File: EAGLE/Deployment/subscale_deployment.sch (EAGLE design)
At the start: 6 parts, among them J1 1935161, J2 1935161, J3 1935161, Q1 100V 14A

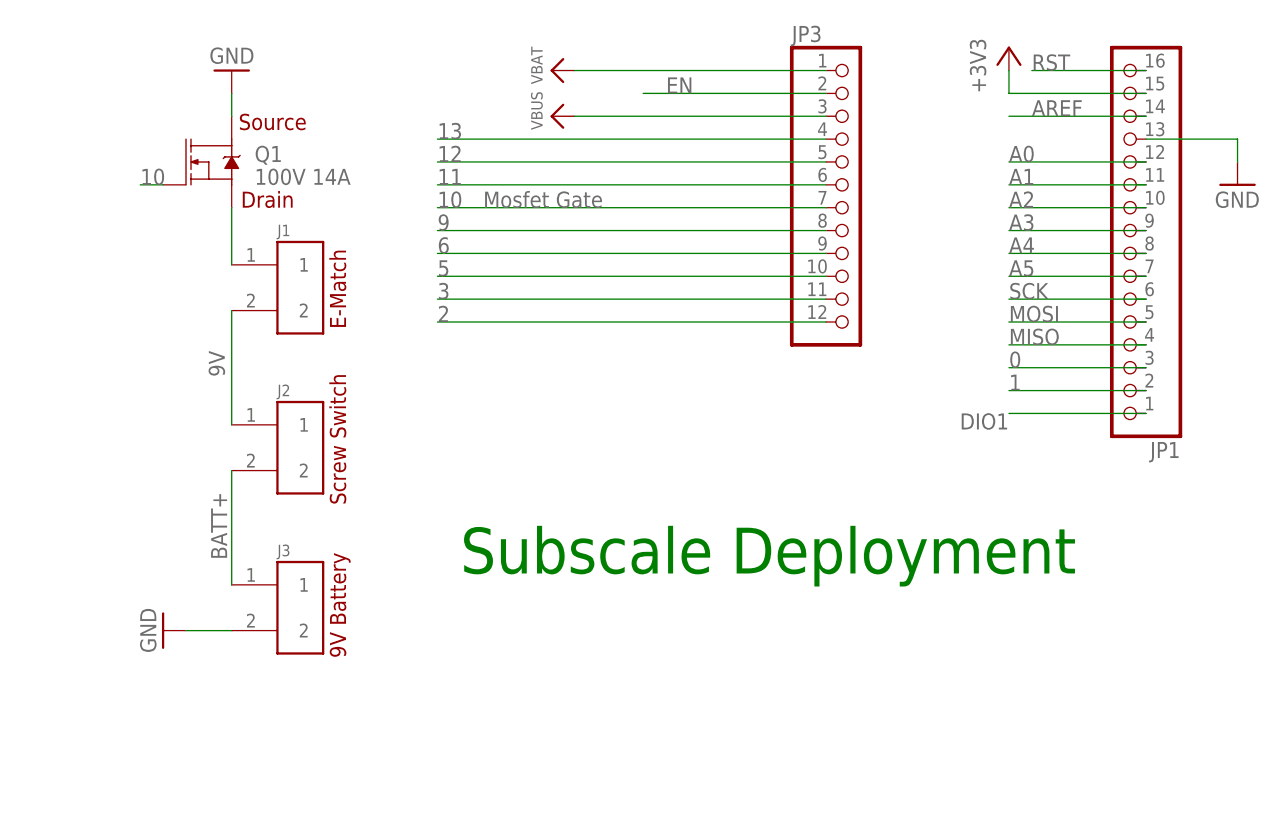
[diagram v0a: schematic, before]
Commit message: Completed layout and routing of subscale deployment PCB
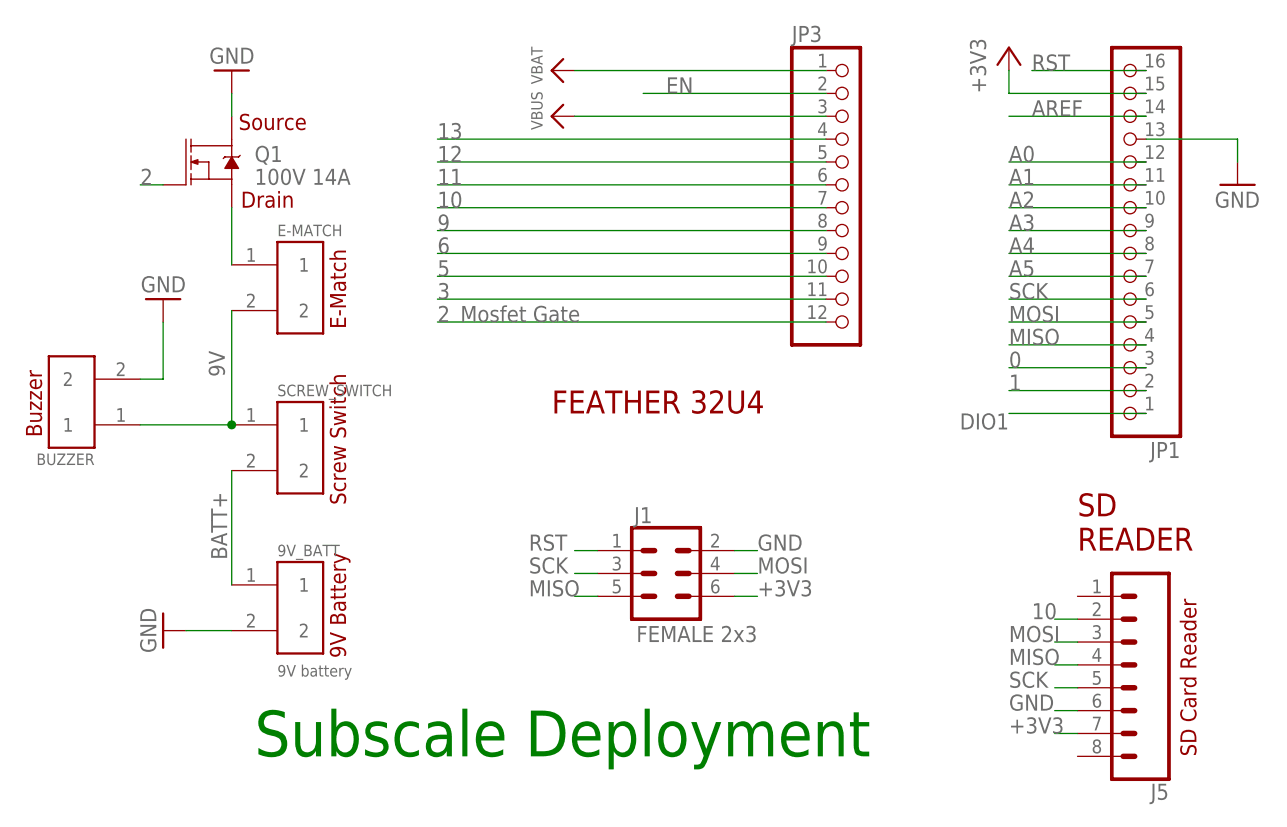
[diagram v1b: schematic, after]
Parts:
- added BUZZER, E-MATCH: 1935161, 1935161:1935161
- added J5: (no value), SparkFun-Connectors:CONN_08"
- 9V_BATT: value 1935161 -> 9V battery
- J1: value 1935161 -> FEMALE 2x3; device 1935161:1935161 -> SparkFun-Connectors:CONN_03X2FEMALE
- renumbered J2 to SCREW_SWITCH, J3 to 9V_BATT
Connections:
- net +3V3: now also J1.6, J5.7
- net 10: now also J5.2; no longer Q1.G
- net 2: now also Q1.G
- net 9V: now also BUZZER.1, E-MATCH.2; no longer J1.2
- net GND: now also BUZZER.2, J1.2, J5.6
- net MISO: now also J1.5, J5.4
- net MOSI: now also J1.4, J5.3
- net N$1: now also E-MATCH.1; no longer J1.1
- net RST: now also J1.1
- net SCK: now also J1.3, J5.5
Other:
- note added: "Buzzer"
- note added: "FEATHER 32U4"
- note added: "SD Card Reader"
- note added: "SD READER"
